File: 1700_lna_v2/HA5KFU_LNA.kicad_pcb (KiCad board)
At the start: 4 copper layers, 35.8 x 15.4 mm, 20 parts, among them J1 Conn_Coaxial, J2 Conn_Coaxial, J3 571-1-826629-2, J4 Conn_01x03_Pin, U1 NCP163ASN330T1G, U2 QPL9547

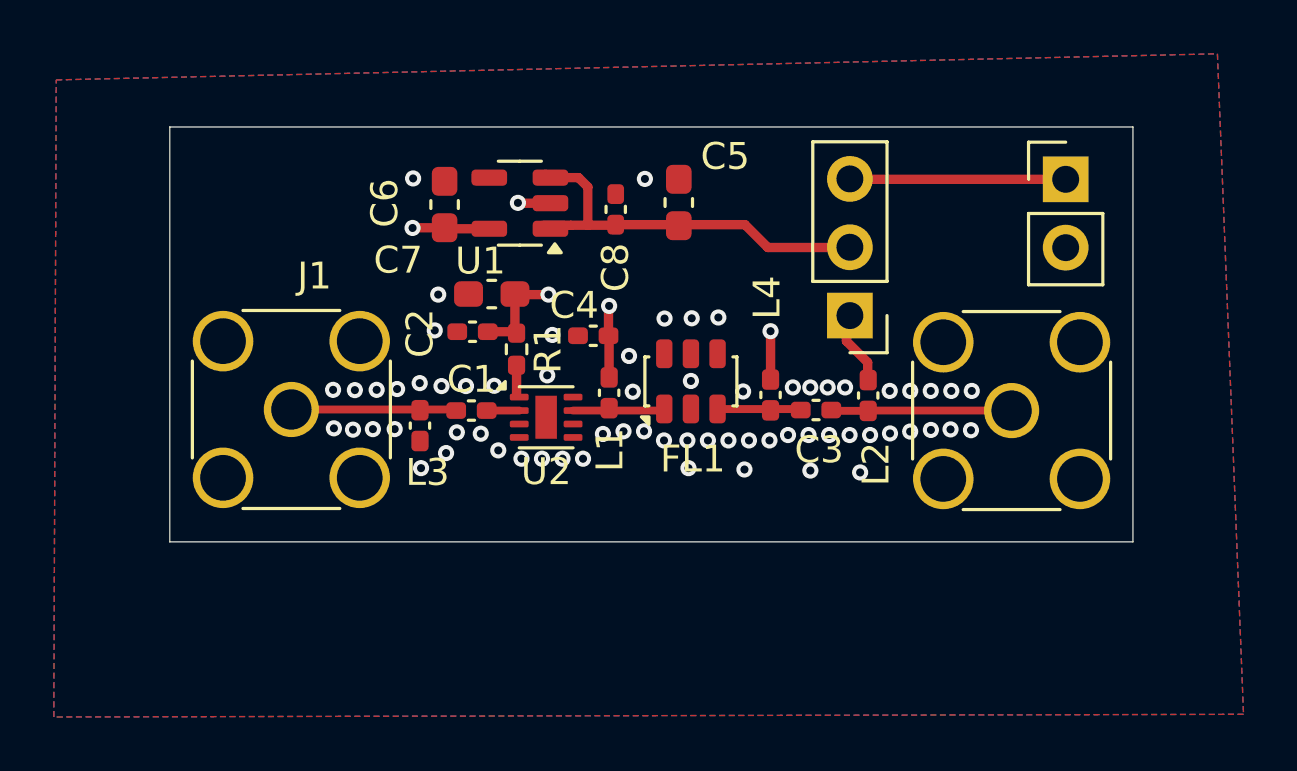
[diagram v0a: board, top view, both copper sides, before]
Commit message: Changed transmission line parameters
Changed transmission line width and ground plane to trace distance to better fit reduce parasitic capacitance.
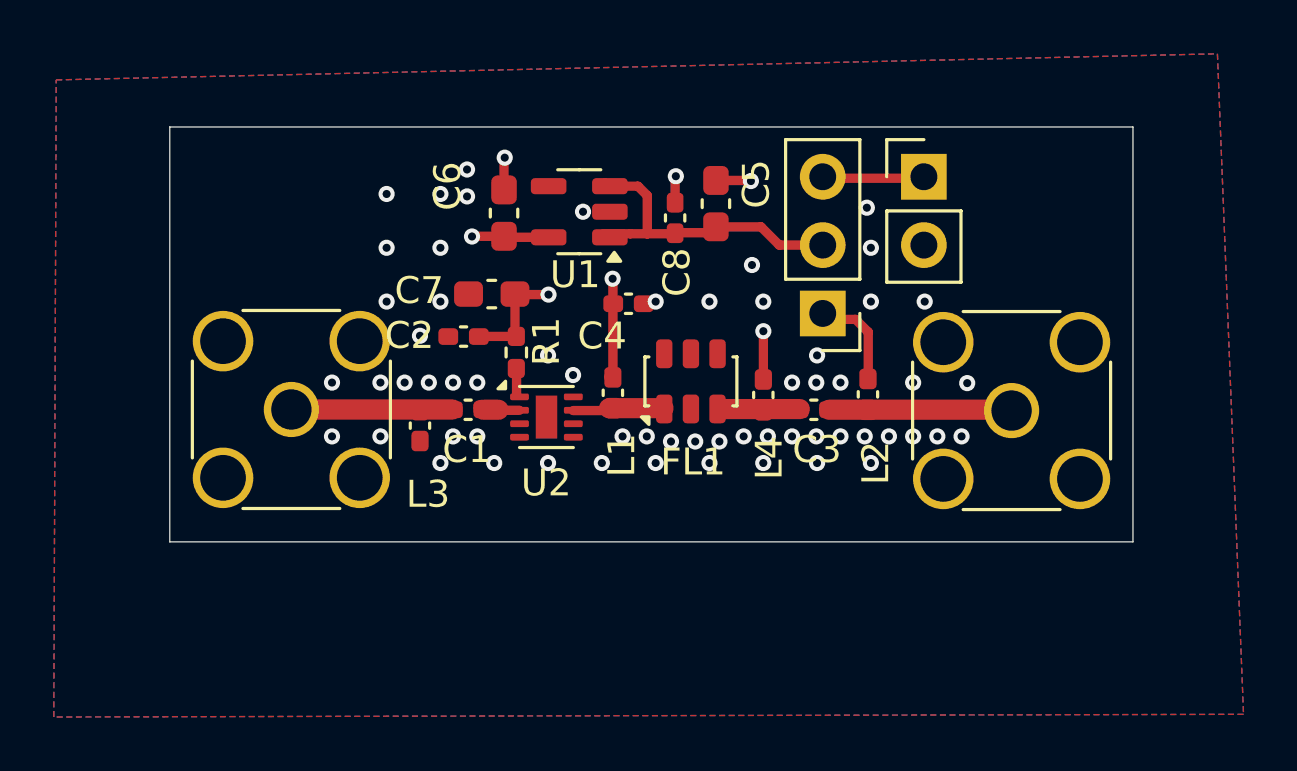
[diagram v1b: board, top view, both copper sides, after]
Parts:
- moved J3 5.27 mm to (141.3, 72.6)
- moved C6 2.23 mm to (125.7, 73.9)
- moved U1 2.23 mm to (128.5, 73.9)
- moved C8 2.23 mm to (132.0, 74.1)
- moved C4 1.77 mm to (130.3, 77.3), turned to 0 degrees
- moved C5 1.38 mm to (133.6, 73.6)
- moved J4 1.01 mm to (137.5, 77.6)
- moved C2 0.38 mm to (124.2, 78.5)
- moved L4 0.27 mm to (135.3, 80.7)
- moved L1 0.14 mm to (129.7, 80.6)
- moved C1 0.13 mm to (124.3, 81.2)
- moved R1 0.12 mm to (126.1, 79.1)
- moved C3 0.08 mm to (137.2, 81.2)
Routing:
- net +5V: track 8.03 -> 4.30 mm
- net Net-(J4-Pin_2): track 15.0 -> 11.8 mm
- net GND: track 1.22 -> 3.51 mm, vias 67 -> 63
- net +3V3: track 11.4 -> 12.7 mm
- net Net-(J4-Pin_1): track 2.79 -> 3.76 mm
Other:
- board text added: "HA5KFU - L_Band LNA 2026 HA7DN, TEX"

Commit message: Removed via from pad
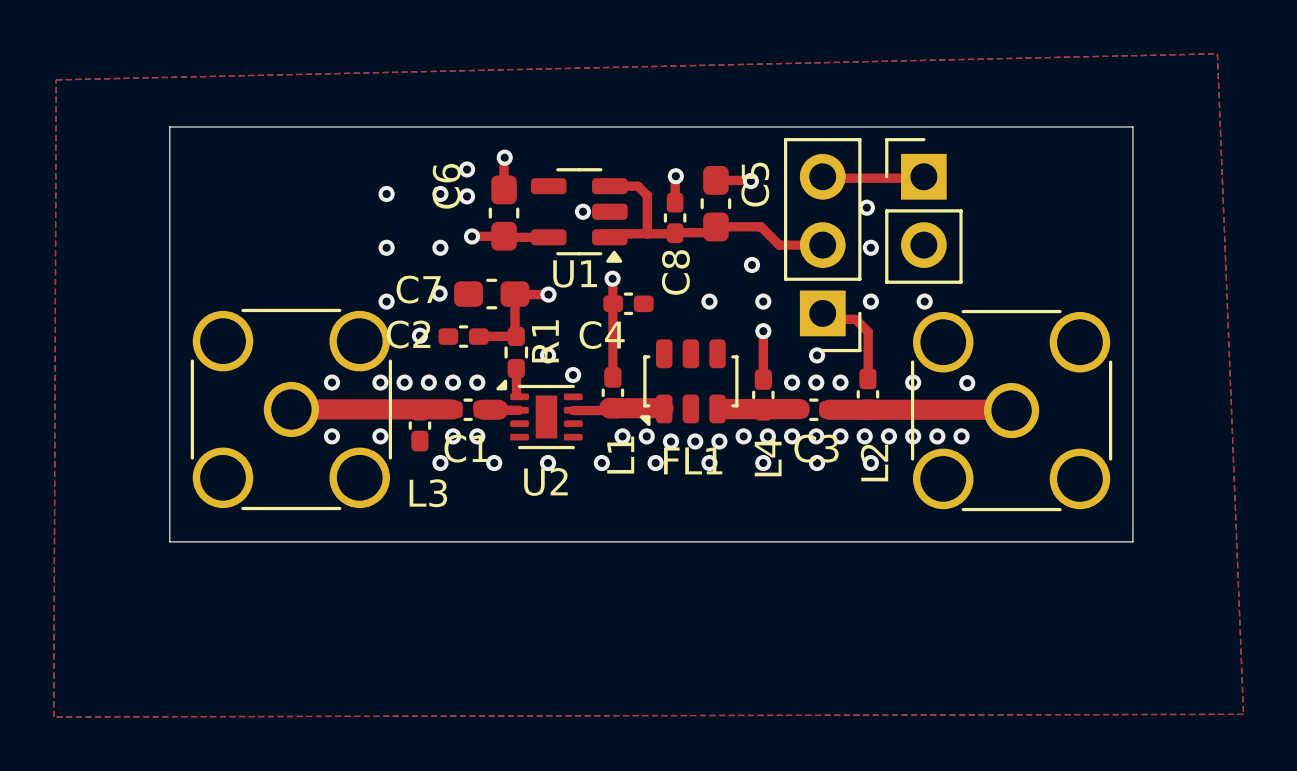
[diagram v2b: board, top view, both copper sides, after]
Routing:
- net GND: vias 63 -> 62
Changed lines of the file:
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@@
-	)
-	(via
-		(at 131.32 77.2)
-		(size 0.6)
-		(drill 0.3)
-		(layers "F.Cu" "B.Cu")
-		(free yes)
-		(net 2)
 	)
 	(via
@@
 	)
 	(via
-		(at 123.32 77.2)
+		(at 123.29 76.9)
 		(size 0.6)
 		(drill 0.3)
